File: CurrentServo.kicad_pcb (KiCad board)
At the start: 2 copper layers, 130 x 85 mm, 102 parts, among them P1 POWER, P2 SENSE, P3 V_DAC, P4 VREF, P5 HH_IN, P6 OUT, SW1 1AS2T2B4M2RE, U1 VHP4Z, U10 TC7650, U11 TC7650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

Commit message: Files sent for manufacture
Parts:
- removed the REF** at (169.5, 61.8)
- removed the REF** at (169.5, 136.8)
- removed the REF** at (49.5, 136.8)
- removed the REF** at (49.5, 61.8)
- added REF**: MountingHole_3-5mm, Mounting_Holes:MountingHole_3-5mm, F.Cu at (49.5, 61.8)
- added REF**: MountingHole_3-5mm, Mounting_Holes:MountingHole_3-5mm, F.Cu at (49.5, 136.8)
- added REF**: MountingHole_3-5mm, Mounting_Holes:MountingHole_3-5mm, F.Cu at (169.5, 136.8)
- added REF**: MountingHole_3-5mm, Mounting_Holes:MountingHole_3-5mm, F.Cu at (169.5, 61.8)
- U6: footprint Opto-Devices:Optocoupler_6pin_wide_Stile-I -> local:TLP116A
- moved P5 2.54 mm to (64.1, 64.0)
- moved R3 0.94 mm to (64.8, 73.5)
- turned U6 to 270 degrees
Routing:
- net VCC: track 190.7 -> 193.1 mm
- net Net-(P5-Pad2): track 21.3 -> 23.7 mm
- net Net-(P5-Pad1): track 7.84 -> 5.46 mm
- net HH_TTL: track 197.3 -> 199.0 mm, vias 3 -> 4
- net Net-(R3-Pad1): track 2.54 -> 4.19 mm
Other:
- board text added: "2016-11-14"

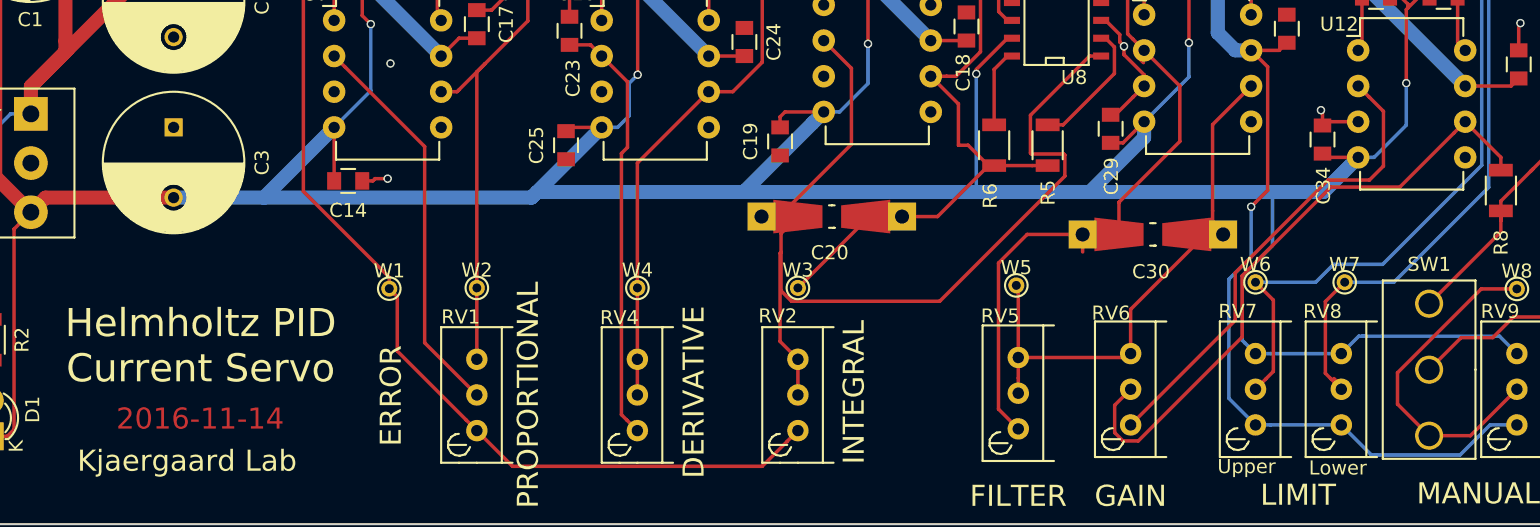
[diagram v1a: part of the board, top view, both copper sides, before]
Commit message: Documented and fixed output gain bug
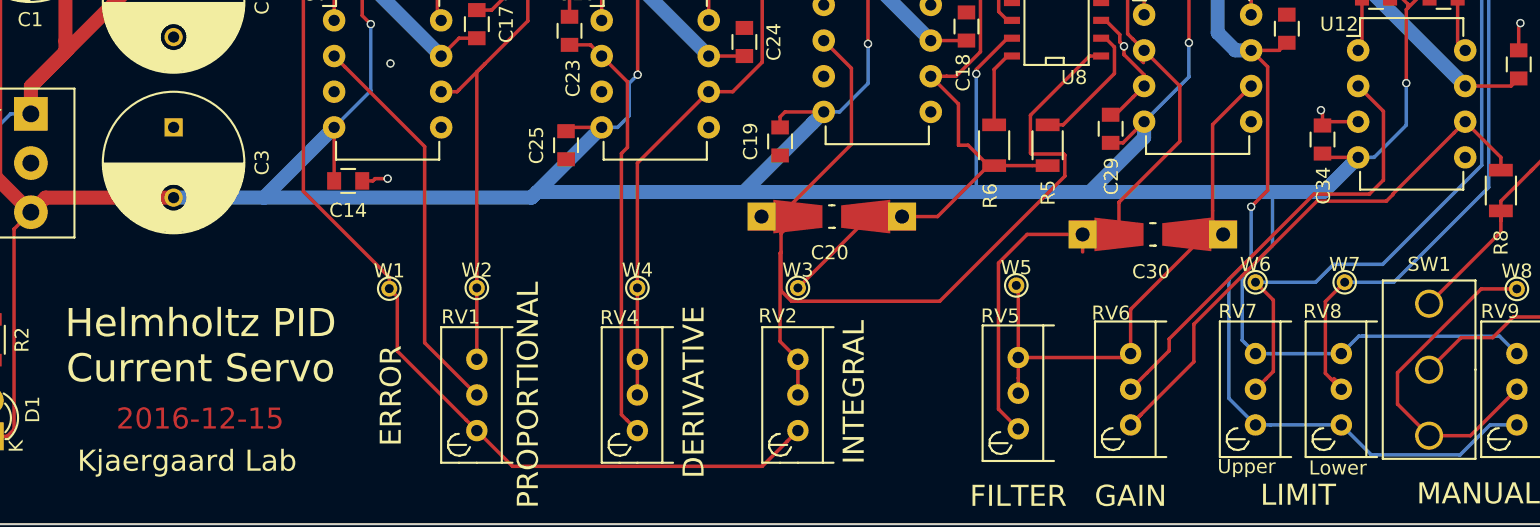
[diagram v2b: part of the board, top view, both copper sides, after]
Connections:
- RV6 pad 1: Net-(RV6-Pad1) -> Net-(R8-Pad2)
- RV6 pad 2: Net-(R8-Pad2) -> Net-(RV6-Pad2)
- U12 pad 2: Net-(RV6-Pad1) -> Net-(RV6-Pad2)
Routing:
- net Net-(RV6-Pad1): track 34.1 -> 0.00 mm
- net Net-(RV6-Pad2): track 0.00 -> 32.1 mm
- net Net-(R8-Pad2): track 45.2 -> 39.9 mm
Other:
- board text added: "2016-12-15"
- board text removed: "2016-11-14"
